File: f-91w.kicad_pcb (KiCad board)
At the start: 4 copper layers, 24.4 x 24.4 mm, 113 parts, among them P1 CONN_01X01, P10 CONN_01X01, P11 CONN_01X01, P13 CONN_01X01, P14 CONN_01X01, P2 CONN_01X01, P3 CONN_01X01, P5 CONN_01X01, P6 CONN_01X01, P7 CONN_01X01, P8 CONN_01X01, P9 CONN_01X01, Q1 BC846, U1 CY8C4248LQI-BL483, U2 LCD-F-91W, U3 BME680, Y1 32.768KHz, Y2 24MHz

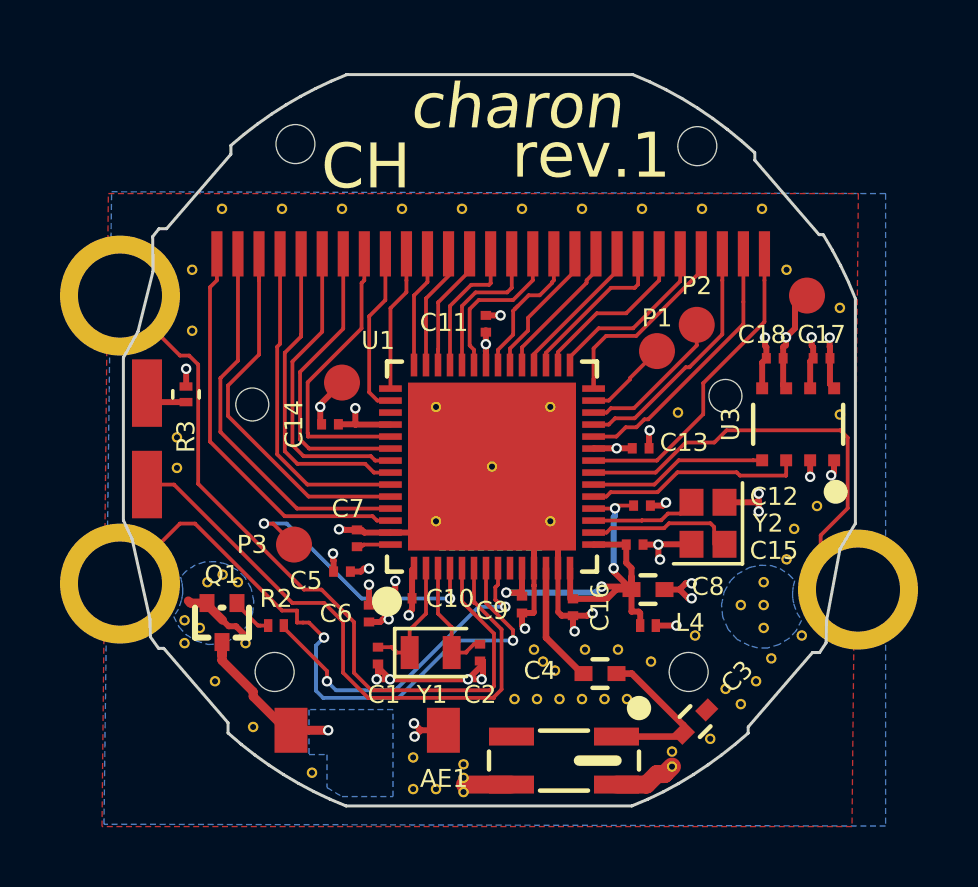
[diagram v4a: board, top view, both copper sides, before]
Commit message: REV1 ISSUE2: Fix all remaining DRC errors, check eurocircuits DFM
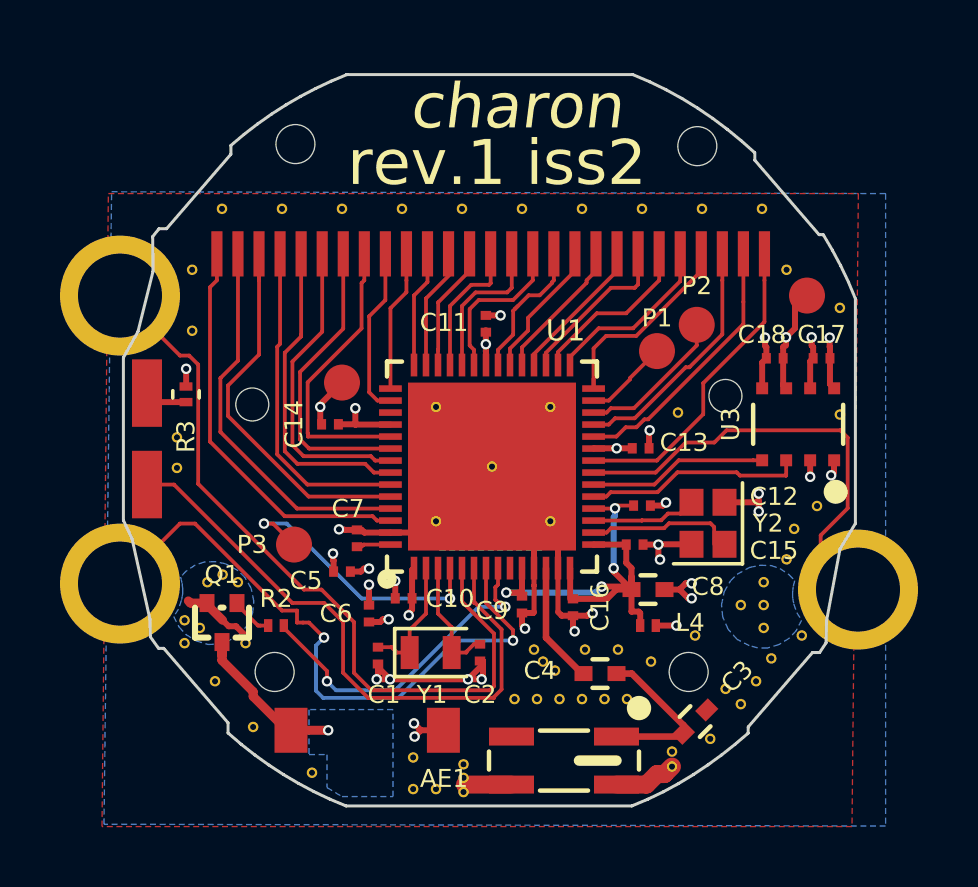
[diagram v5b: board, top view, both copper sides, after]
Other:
- board text added: "rev.1 iss2"
- board text removed: "CH"
- board text removed: "rev.1"

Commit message: Increase annular ring for all vias to 0.127mm
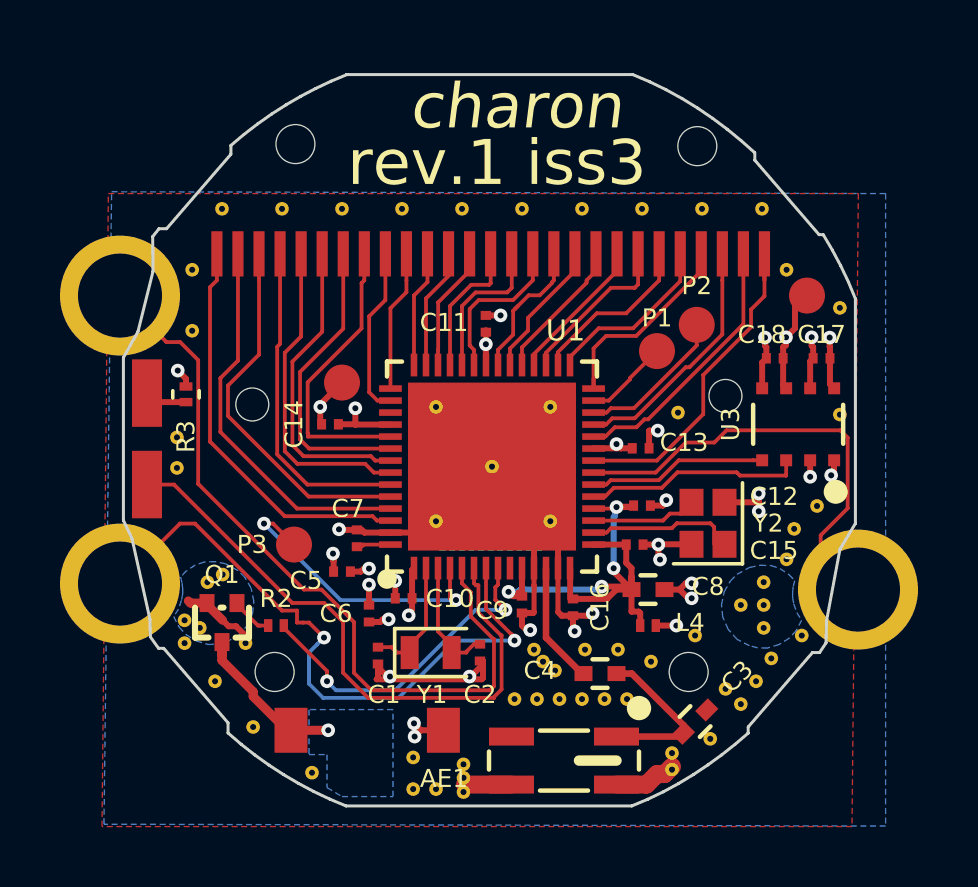
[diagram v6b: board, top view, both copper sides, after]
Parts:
- removed the REF** at (49.5, 101.9)
- moved REF** 0.10 mm to (64.0, 108.1)
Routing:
- net /LCD_SEG24: track 10.5 -> 11.4 mm
- net VDDR: track 17.9 -> 18.5 mm
- net GND: track 47.0 -> 47.3 mm, vias 24 -> 22
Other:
- net class ANT: via_dia 0.35 -> 0.454
- net class Default: via_dia 0.35 -> 0.454
- net class PWR: via_dia 0.35 -> 0.454
- rule via_min_size: 0.2 -> 0.454
- board text added: "rev.1 iss3"
- board text removed: "rev.1 iss2"
